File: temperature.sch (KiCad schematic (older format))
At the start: 20 parts, among them T1+1 TestPoint, T1-1 TestPoint, T2+1 TestPoint, T2-1 TestPoint, U4 ADS1118IDGS

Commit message: Debug routing
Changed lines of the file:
@@
 $Descr A4 11693 8268
 encoding utf-8
-Sheet 58 80
+Sheet 2 80
 Title "Acquisiton température"
 Date "2020-05-19"
@@
 AR Path="/5F466B56/5EB520F2" Ref="U34"  Part="1"
 AR Path="/5F466B61/5EB520F2" Ref="U35"  Part="1"
-F 0 "U35" H 7250 4400 50  0000 C CNN
+F 0 "U4" H 7250 4400 50  0000 C CNN
 F 1 "ADS1118IDGS" H 7250 4300 50  0000 C CNN
 F 2 "Package_SO:VSSOP-10_3x3mm_P0.5mm" H 6900 3750 50  0001 C CNN
@@
 AR Path="/5F466B56/5EC3D85A" Ref="C90"  Part="1"
 AR Path="/5F466B61/5EC3D85A" Ref="C97"  Part="1"
-F 0 "C97" H 5365 4896 50  0000 L CNN
+F 0 "C14" H 5365 4896 50  0000 L CNN
 F 1 "1uF" H 5365 4805 50  0000 L CNN
 F 2 "Capacitor_SMD:C_0402_1005Metric" H 5288 4700 50  0001 C CNN
@@
 AR Path="/5F466B56/5EC3D854" Ref="C88"  Part="1"
 AR Path="/5F466B61/5EC3D854" Ref="C95"  Part="1"
-F 0 "C95" H 5165 5346 50  0000 L CNN
+F 0 "C12" H 5165 5346 50  0000 L CNN
 F 1 "0.1uF" H 5165 5255 50  0000 L CNN
 F 2 "Capacitor_SMD:C_0402_1005Metric" H 5088 5150 50  0001 C CNN
@@
 AR Path="/5F466B56/5EC3D84E" Ref="C87"  Part="1"
 AR Path="/5F466B61/5EC3D84E" Ref="C94"  Part="1"
-F 0 "C94" H 4935 4354 50  0000 R CNN
+F 0 "C11" H 4935 4354 50  0000 R CNN
 F 1 "0.1uF" H 4935 4445 50  0000 R CNN
 F 2 "Capacitor_SMD:C_0402_1005Metric" H 5088 4250 50  0001 C CNN
@@
 AR Path="/5F466B56/5EC3D848" Ref="R116"  Part="1"
 AR Path="/5F466B61/5EC3D848" Ref="R124"  Part="1"
-F 0 "R124" V 4443 4650 50  0000 C CNN
+F 0 "R12" V 4443 4650 50  0000 C CNN
 F 1 "499" V 4534 4650 50  0000 C CNN
 F 2 "Resistor_SMD:R_0603_1608Metric" V 4580 4650 50  0001 C CNN
@@
 AR Path="/5F466B56/5EC3D842" Ref="R117"  Part="1"
 AR Path="/5F466B61/5EC3D842" Ref="R125"  Part="1"
-F 0 "R125" V 4443 5050 50  0000 C CNN
+F 0 "R13" V 4443 5050 50  0000 C CNN
 F 1 "499" V 4534 5050 50  0000 C CNN
 F 2 "Resistor_SMD:R_0603_1608Metric" V 4580 5050 50  0001 C CNN
@@
 AR Path="/5F466B56/5EC3D83C" Ref="R113"  Part="1"
 AR Path="/5F466B61/5EC3D83C" Ref="R121"  Part="1"
-F 0 "R121" H 4120 5346 50  0000 L CNN
+F 0 "R9" H 4120 5346 50  0000 L CNN
 F 1 "1M" H 4120 5255 50  0000 L CNN
 F 2 "Resistor_SMD:R_0805_2012Metric" V 3980 5300 50  0001 C CNN
@@
 AR Path="/5F466B56/5EC3D836" Ref="R112"  Part="1"
 AR Path="/5F466B61/5EC3D836" Ref="R120"  Part="1"
-F 0 "R120" H 4120 4446 50  0000 L CNN
+F 0 "R8" H 4120 4446 50  0000 L CNN
 F 1 "1M" H 4120 4355 50  0000 L CNN
 F 2 "Resistor_SMD:R_0805_2012Metric" V 3980 4400 50  0001 C CNN
@@
 AR Path="/5F466B56/5EBEC841" Ref="C91"  Part="1"
 AR Path="/5F466B61/5EBEC841" Ref="C98"  Part="1"
-F 0 "C98" H 6850 2950 50  0000 C CNN
+F 0 "C15" H 6850 2950 50  0000 C CNN
 F 1 "0.1uF" H 6850 3050 50  0000 C CNN
 F 2 "Capacitor_SMD:C_0402_1005Metric" H 6638 2850 50  0001 C CNN
@@
 AR Path="/5F466B56/5EC2636D" Ref="T2+7"  Part="1"
 AR Path="/5F466B61/5EC2636D" Ref="T2+8"  Part="1"
-F 0 "T2+8" H 4458 4368 50  0000 L CNN
+F 0 "T2+1" H 4458 4368 50  0000 L CNN
 F 1 "TestPoint" H 4458 4277 50  0000 L CNN
 F 2 "TestPoint:TestPoint_Pad_1.0x1.0mm" H 4600 4250 50  0001 C CNN
@@
 AR Path="/5F466B56/5EC467A6" Ref="T2-7"  Part="1"
 AR Path="/5F466B61/5EC467A6" Ref="T2-8"  Part="1"
-F 0 "T2-8" H 4050 5600 50  0000 L CNN
+F 0 "T2-1" H 4050 5600 50  0000 L CNN
 F 1 "TestPoint" H 4000 5500 50  0000 L CNN
 F 2 "TestPoint:TestPoint_Pad_1.0x1.0mm" H 4600 5450 50  0001 C CNN
@@
 AR Path="/5F466B56/5EC22011" Ref="T1-7"  Part="1"
 AR Path="/5F466B61/5EC22011" Ref="T1-8"  Part="1"
-F 0 "T1-8" H 4050 3500 50  0000 L CNN
+F 0 "T1-1" H 4050 3500 50  0000 L CNN
 F 1 "TestPoint" H 4000 3400 50  0000 L CNN
 F 2 "TestPoint:TestPoint_Pad_1.0x1.0mm" H 4600 3350 50  0001 C CNN
@@
 AR Path="/5F466B56/5EC1E92D" Ref="T1+7"  Part="1"
 AR Path="/5F466B61/5EC1E92D" Ref="T1+8"  Part="1"
-F 0 "T1+8" H 4458 2268 50  0000 L CNN
+F 0 "T1+1" H 4458 2268 50  0000 L CNN
 F 1 "TestPoint" H 4458 2177 50  0000 L CNN
 F 2 "TestPoint:TestPoint_Pad_1.0x1.0mm" H 4600 2150 50  0001 C CNN
@@
 AR Path="/5F466B56/5EC09C7B" Ref="R110"  Part="1"
 AR Path="/5F466B61/5EC09C7B" Ref="R118"  Part="1"
-F 0 "R118" H 4120 2346 50  0000 L CNN
+F 0 "R6" H 4120 2346 50  0000 L CNN
 F 1 "1M" H 4120 2255 50  0000 L CNN
 F 2 "Resistor_SMD:R_0805_2012Metric" V 3980 2300 50  0001 C CNN
@@
 AR Path="/5F466B56/5EC0F883" Ref="R111"  Part="1"
 AR Path="/5F466B61/5EC0F883" Ref="R119"  Part="1"
-F 0 "R119" H 4120 3246 50  0000 L CNN
+F 0 "R7" H 4120 3246 50  0000 L CNN
 F 1 "1M" H 4120 3155 50  0000 L CNN
 F 2 "Resistor_SMD:R_0805_2012Metric" V 3980 3200 50  0001 C CNN
@@
 AR Path="/5F466B56/5EC11D48" Ref="R115"  Part="1"
 AR Path="/5F466B61/5EC11D48" Ref="R123"  Part="1"
-F 0 "R123" V 4443 2950 50  0000 C CNN
+F 0 "R11" V 4443 2950 50  0000 C CNN
 F 1 "499" V 4534 2950 50  0000 C CNN
 F 2 "Resistor_SMD:R_0603_1608Metric" V 4580 2950 50  0001 C CNN
@@
 AR Path="/5F466B56/5EC12ACC" Ref="R114"  Part="1"
 AR Path="/5F466B61/5EC12ACC" Ref="R122"  Part="1"
-F 0 "R122" V 4443 2550 50  0000 C CNN
+F 0 "R10" V 4443 2550 50  0000 C CNN
 F 1 "499" V 4534 2550 50  0000 C CNN
 F 2 "Resistor_SMD:R_0603_1608Metric" V 4580 2550 50  0001 C CNN
@@
 AR Path="/5F466B56/5EC13396" Ref="C85"  Part="1"
 AR Path="/5F466B61/5EC13396" Ref="C92"  Part="1"
-F 0 "C92" H 4935 2254 50  0000 R CNN
+F 0 "C9" H 4935 2254 50  0000 R CNN
 F 1 "0.1uF" H 4935 2345 50  0000 R CNN
 F 2 "Capacitor_SMD:C_0402_1005Metric" H 5088 2150 50  0001 C CNN
@@
 AR Path="/5F466B56/5EC146F1" Ref="C86"  Part="1"
 AR Path="/5F466B61/5EC146F1" Ref="C93"  Part="1"
-F 0 "C93" H 5165 3246 50  0000 L CNN
+F 0 "C10" H 5165 3246 50  0000 L CNN
 F 1 "0.1uF" H 5165 3155 50  0000 L CNN
 F 2 "Capacitor_SMD:C_0402_1005Metric" H 5088 3050 50  0001 C CNN
@@
 AR Path="/5F466B56/5EC15202" Ref="C89"  Part="1"
 AR Path="/5F466B61/5EC15202" Ref="C96"  Part="1"
-F 0 "C96" H 5365 2796 50  0000 L CNN
+F 0 "C13" H 5365 2796 50  0000 L CNN
 F 1 "1uF" H 5365 2705 50  0000 L CNN
 F 2 "Capacitor_SMD:C_0402_1005Metric" H 5288 2600 50  0001 C CNN
@@
 AR Path="/5F466B56/618455B5" Ref="#PWR0188"  Part="1"
 AR Path="/5F466B61/618455B5" Ref="#PWR0196"  Part="1"
-F 0 "#PWR0196" H 6950 4200 50  0001 C CNN
+F 0 "#PWR028" H 6950 4200 50  0001 C CNN
 F 1 "GNDA" H 6955 4277 50  0000 C CNN
 F 2 "" H 6950 4450 50  0001 C CNN
@@
 AR Path="/5F466B56/61845768" Ref="#PWR0187"  Part="1"
 AR Path="/5F466B61/61845768" Ref="#PWR0195"  Part="1"
-F 0 "#PWR0195" H 6600 2900 50  0001 C CNN
+F 0 "#PWR027" H 6600 2900 50  0001 C CNN
 F 1 "GNDA" H 6605 2977 50  0000 C CNN
 F 2 "" H 6600 3150 50  0001 C CNN
@@
 AR Path="/5F466B56/61845B4A" Ref="#PWR0186"  Part="1"
 AR Path="/5F466B61/61845B4A" Ref="#PWR0194"  Part="1"
-F 0 "#PWR0194" H 5050 5200 50  0001 C CNN
+F 0 "#PWR026" H 5050 5200 50  0001 C CNN
 F 1 "GNDA" H 5055 5277 50  0000 C CNN
 F 2 "" H 5050 5450 50  0001 C CNN
@@
 AR Path="/5F466B56/61846A90" Ref="#PWR0182"  Part="1"
 AR Path="/5F466B61/61846A90" Ref="#PWR0190"  Part="1"
-F 0 "#PWR0190" H 4050 5200 50  0001 C CNN
+F 0 "#PWR022" H 4050 5200 50  0001 C CNN
 F 1 "GNDA" H 4055 5277 50  0000 C CNN
 F 2 "" H 4050 5450 50  0001 C CNN
@@
 AR Path="/5F466B56/61846F48" Ref="#PWR0184"  Part="1"
 AR Path="/5F466B61/61846F48" Ref="#PWR0192"  Part="1"
-F 0 "#PWR0192" H 5050 3100 50  0001 C CNN
+F 0 "#PWR024" H 5050 3100 50  0001 C CNN
 F 1 "GNDA" H 5055 3177 50  0000 C CNN
 F 2 "" H 5050 3350 50  0001 C CNN
@@
 AR Path="/5F466B56/618474E2" Ref="#PWR0181"  Part="1"
 AR Path="/5F466B61/618474E2" Ref="#PWR0189"  Part="1"
-F 0 "#PWR0189" H 4050 3100 50  0001 C CNN
+F 0 "#PWR021" H 4050 3100 50  0001 C CNN
 F 1 "GNDA" H 4055 3177 50  0000 C CNN
 F 2 "" H 4050 3350 50  0001 C CNN
@@
 AR Path="/5F466B56/6184779B" Ref="#PWR0185"  Part="1"
 AR Path="/5F466B61/6184779B" Ref="#PWR0193"  Part="1"
-F 0 "#PWR0193" H 5050 4000 50  0001 C CNN
+F 0 "#PWR025" H 5050 4000 50  0001 C CNN
 F 1 "GNDA" H 5055 4077 50  0000 C CNN
 F 2 "" H 5050 4250 50  0001 C CNN
@@
 AR Path="/5F466B56/6184B7DC" Ref="#PWR0183"  Part="1"
 AR Path="/5F466B61/6184B7DC" Ref="#PWR0191"  Part="1"
-F 0 "#PWR0191" H 5050 1900 50  0001 C CNN
+F 0 "#PWR023" H 5050 1900 50  0001 C CNN
 F 1 "GNDA" H 5055 1977 50  0000 C CNN
 F 2 "" H 5050 2150 50  0001 C CNN

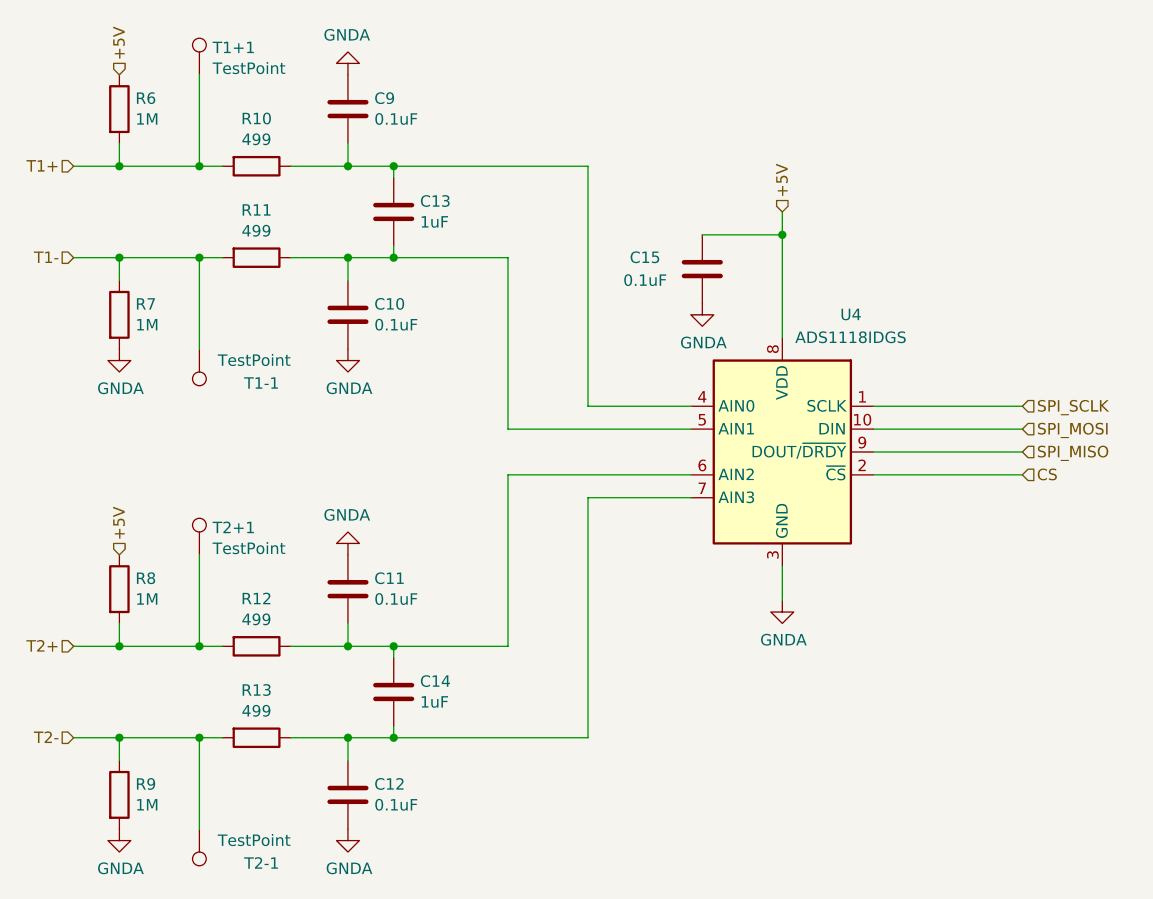
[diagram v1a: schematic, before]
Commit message: retrait des test points inutiles
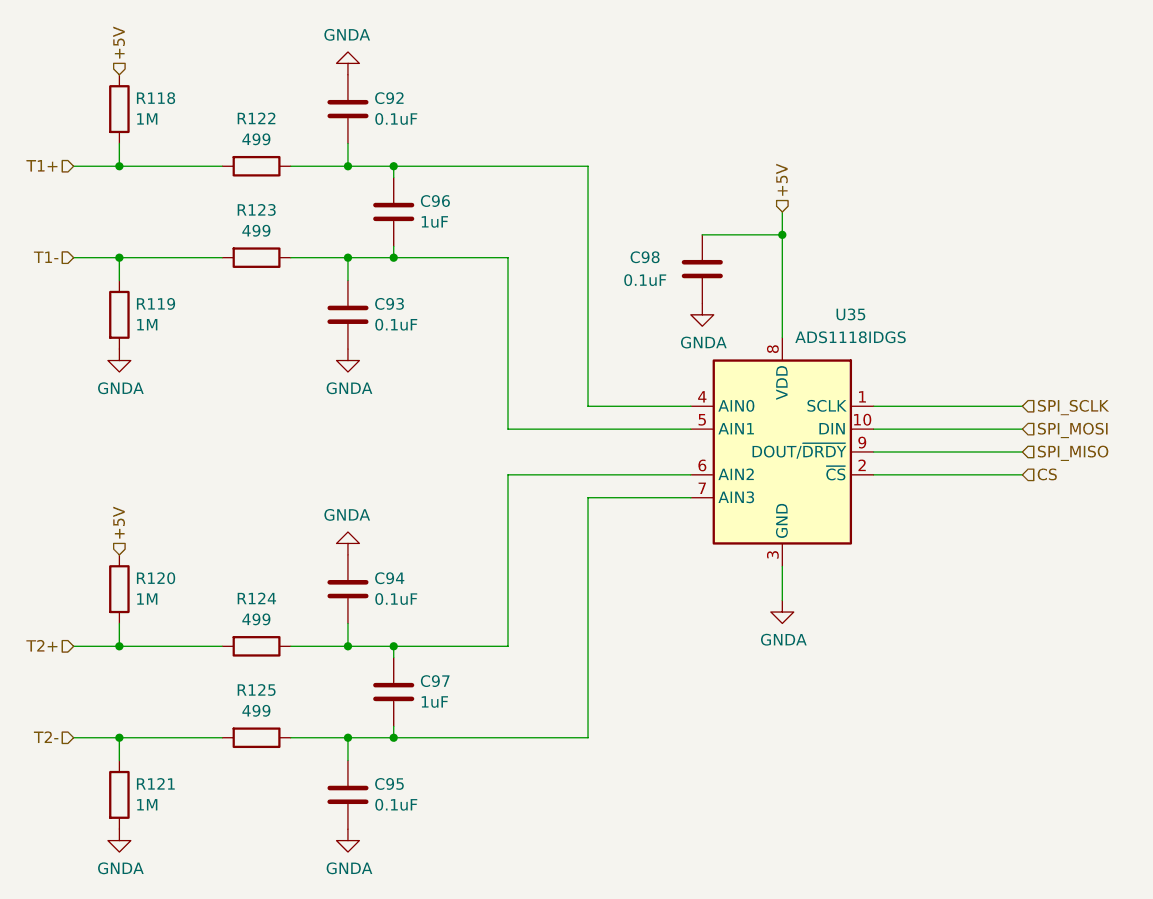
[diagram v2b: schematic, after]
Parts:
- removed T1+1, T1-1, T2+1, T2-1: TestPoint, TestPoint:TestPoint_Pad_1.0x1.0mm, symbol Connector:TestPoint

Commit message: Routed most of the power
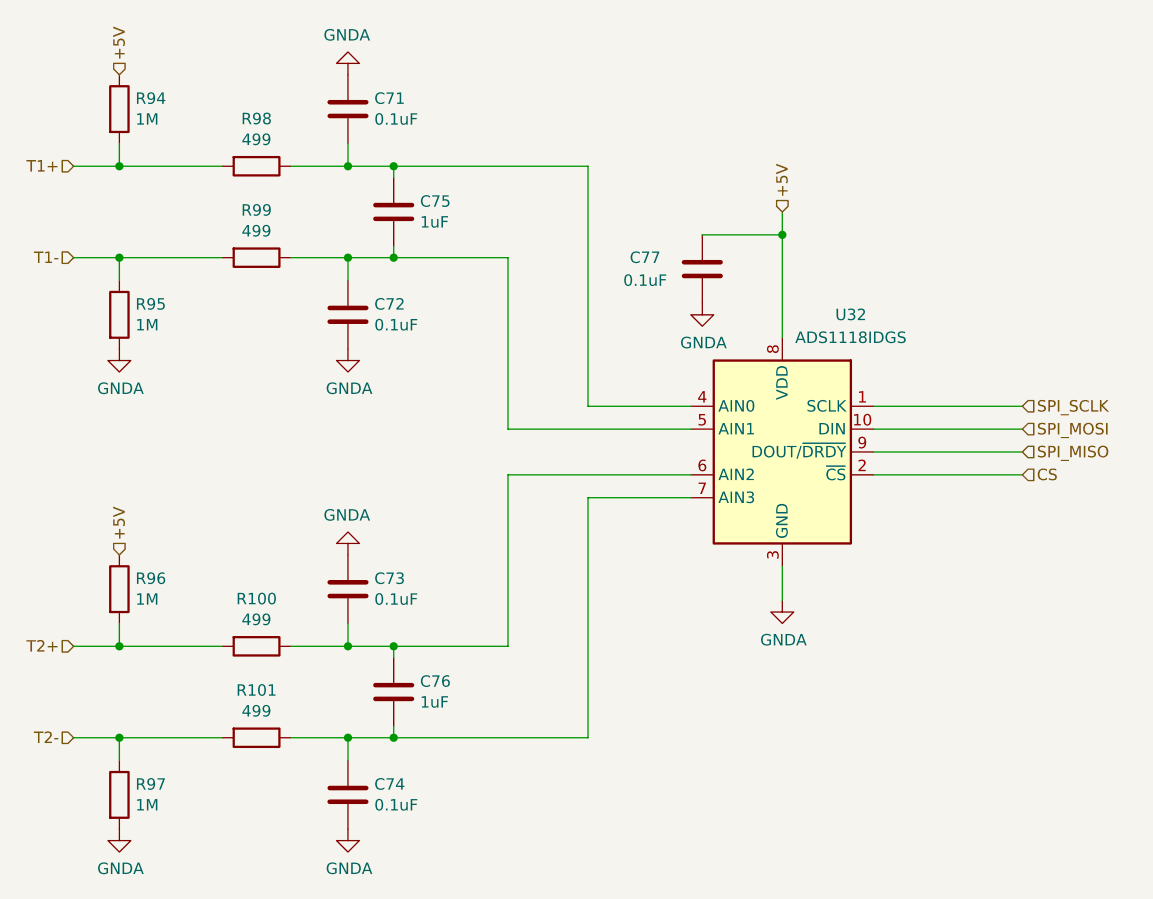
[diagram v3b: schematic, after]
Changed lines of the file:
@@
 $Descr A4 11693 8268
 encoding utf-8
-Sheet 2 80
+Sheet 55 80
 Title "Acquisiton température"
 Date "2020-05-19"
@@
 AR Path="/5F466B56/5EB520F2" Ref="U34"  Part="1"
 AR Path="/5F466B61/5EB520F2" Ref="U35"  Part="1"
-F 0 "U35" H 7250 4400 50  0000 C CNN
+F 0 "U32" H 7250 4400 50  0000 C CNN
 F 1 "ADS1118IDGS" H 7250 4300 50  0000 C CNN
 F 2 "Package_SO:VSSOP-10_3x3mm_P0.5mm" H 6900 3750 50  0001 C CNN
@@
 AR Path="/5F466B56/5EC3D85A" Ref="C90"  Part="1"
 AR Path="/5F466B61/5EC3D85A" Ref="C97"  Part="1"
-F 0 "C97" H 5365 4896 50  0000 L CNN
+F 0 "C76" H 5365 4896 50  0000 L CNN
 F 1 "1uF" H 5365 4805 50  0000 L CNN
 F 2 "Capacitor_SMD:C_0402_1005Metric" H 5288 4700 50  0001 C CNN
@@
 AR Path="/5F466B56/5EC3D854" Ref="C88"  Part="1"
 AR Path="/5F466B61/5EC3D854" Ref="C95"  Part="1"
-F 0 "C95" H 5165 5346 50  0000 L CNN
+F 0 "C74" H 5165 5346 50  0000 L CNN
 F 1 "0.1uF" H 5165 5255 50  0000 L CNN
 F 2 "Capacitor_SMD:C_0402_1005Metric" H 5088 5150 50  0001 C CNN
@@
 AR Path="/5F466B56/5EC3D84E" Ref="C87"  Part="1"
 AR Path="/5F466B61/5EC3D84E" Ref="C94"  Part="1"
-F 0 "C94" H 4935 4354 50  0000 R CNN
+F 0 "C73" H 4935 4354 50  0000 R CNN
 F 1 "0.1uF" H 4935 4445 50  0000 R CNN
 F 2 "Capacitor_SMD:C_0402_1005Metric" H 5088 4250 50  0001 C CNN
@@
 AR Path="/5F466B56/5EC3D848" Ref="R116"  Part="1"
 AR Path="/5F466B61/5EC3D848" Ref="R124"  Part="1"
-F 0 "R124" V 4443 4650 50  0000 C CNN
+F 0 "R100" V 4443 4650 50  0000 C CNN
 F 1 "499" V 4534 4650 50  0000 C CNN
 F 2 "Resistor_SMD:R_0603_1608Metric" V 4580 4650 50  0001 C CNN
@@
 AR Path="/5F466B56/5EC3D842" Ref="R117"  Part="1"
 AR Path="/5F466B61/5EC3D842" Ref="R125"  Part="1"
-F 0 "R125" V 4443 5050 50  0000 C CNN
+F 0 "R101" V 4443 5050 50  0000 C CNN
 F 1 "499" V 4534 5050 50  0000 C CNN
 F 2 "Resistor_SMD:R_0603_1608Metric" V 4580 5050 50  0001 C CNN
@@
 AR Path="/5F466B56/5EC3D83C" Ref="R113"  Part="1"
 AR Path="/5F466B61/5EC3D83C" Ref="R121"  Part="1"
-F 0 "R121" H 4120 5346 50  0000 L CNN
+F 0 "R97" H 4120 5346 50  0000 L CNN
 F 1 "1M" H 4120 5255 50  0000 L CNN
 F 2 "Resistor_SMD:R_0805_2012Metric" V 3980 5300 50  0001 C CNN
@@
 AR Path="/5F466B56/5EC3D836" Ref="R112"  Part="1"
 AR Path="/5F466B61/5EC3D836" Ref="R120"  Part="1"
-F 0 "R120" H 4120 4446 50  0000 L CNN
+F 0 "R96" H 4120 4446 50  0000 L CNN
 F 1 "1M" H 4120 4355 50  0000 L CNN
 F 2 "Resistor_SMD:R_0805_2012Metric" V 3980 4400 50  0001 C CNN
@@
 AR Path="/5F466B56/5EBEC841" Ref="C91"  Part="1"
 AR Path="/5F466B61/5EBEC841" Ref="C98"  Part="1"
-F 0 "C98" H 6850 2950 50  0000 C CNN
+F 0 "C77" H 6850 2950 50  0000 C CNN
 F 1 "0.1uF" H 6850 3050 50  0000 C CNN
 F 2 "Capacitor_SMD:C_0402_1005Metric" H 6638 2850 50  0001 C CNN
@@
 AR Path="/5F466B56/5EC09C7B" Ref="R110"  Part="1"
 AR Path="/5F466B61/5EC09C7B" Ref="R118"  Part="1"
-F 0 "R118" H 4120 2346 50  0000 L CNN
+F 0 "R94" H 4120 2346 50  0000 L CNN
 F 1 "1M" H 4120 2255 50  0000 L CNN
 F 2 "Resistor_SMD:R_0805_2012Metric" V 3980 2300 50  0001 C CNN
@@
 AR Path="/5F466B56/5EC0F883" Ref="R111"  Part="1"
 AR Path="/5F466B61/5EC0F883" Ref="R119"  Part="1"
-F 0 "R119" H 4120 3246 50  0000 L CNN
+F 0 "R95" H 4120 3246 50  0000 L CNN
 F 1 "1M" H 4120 3155 50  0000 L CNN
 F 2 "Resistor_SMD:R_0805_2012Metric" V 3980 3200 50  0001 C CNN
@@
 AR Path="/5F466B56/5EC11D48" Ref="R115"  Part="1"
 AR Path="/5F466B61/5EC11D48" Ref="R123"  Part="1"
-F 0 "R123" V 4443 2950 50  0000 C CNN
+F 0 "R99" V 4443 2950 50  0000 C CNN
 F 1 "499" V 4534 2950 50  0000 C CNN
 F 2 "Resistor_SMD:R_0603_1608Metric" V 4580 2950 50  0001 C CNN
@@
 AR Path="/5F466B56/5EC12ACC" Ref="R114"  Part="1"
 AR Path="/5F466B61/5EC12ACC" Ref="R122"  Part="1"
-F 0 "R122" V 4443 2550 50  0000 C CNN
+F 0 "R98" V 4443 2550 50  0000 C CNN
 F 1 "499" V 4534 2550 50  0000 C CNN
 F 2 "Resistor_SMD:R_0603_1608Metric" V 4580 2550 50  0001 C CNN
@@
 AR Path="/5F466B56/5EC13396" Ref="C85"  Part="1"
 AR Path="/5F466B61/5EC13396" Ref="C92"  Part="1"
-F 0 "C92" H 4935 2254 50  0000 R CNN
+F 0 "C71" H 4935 2254 50  0000 R CNN
 F 1 "0.1uF" H 4935 2345 50  0000 R CNN
 F 2 "Capacitor_SMD:C_0402_1005Metric" H 5088 2150 50  0001 C CNN
@@
 AR Path="/5F466B56/5EC146F1" Ref="C86"  Part="1"
 AR Path="/5F466B61/5EC146F1" Ref="C93"  Part="1"
-F 0 "C93" H 5165 3246 50  0000 L CNN
+F 0 "C72" H 5165 3246 50  0000 L CNN
 F 1 "0.1uF" H 5165 3155 50  0000 L CNN
 F 2 "Capacitor_SMD:C_0402_1005Metric" H 5088 3050 50  0001 C CNN
@@
 AR Path="/5F466B56/5EC15202" Ref="C89"  Part="1"
 AR Path="/5F466B61/5EC15202" Ref="C96"  Part="1"
-F 0 "C96" H 5365 2796 50  0000 L CNN
+F 0 "C75" H 5365 2796 50  0000 L CNN
 F 1 "1uF" H 5365 2705 50  0000 L CNN
 F 2 "Capacitor_SMD:C_0402_1005Metric" H 5288 2600 50  0001 C CNN
@@
 AR Path="/5F466B56/618455B5" Ref="#PWR0188"  Part="1"
 AR Path="/5F466B61/618455B5" Ref="#PWR0196"  Part="1"
-F 0 "#PWR0196" H 6950 4200 50  0001 C CNN
+F 0 "#PWR0172" H 6950 4200 50  0001 C CNN
 F 1 "GNDA" H 6955 4277 50  0000 C CNN
 F 2 "" H 6950 4450 50  0001 C CNN
@@
 AR Path="/5F466B56/61845768" Ref="#PWR0187"  Part="1"
 AR Path="/5F466B61/61845768" Ref="#PWR0195"  Part="1"
-F 0 "#PWR0195" H 6600 2900 50  0001 C CNN
+F 0 "#PWR0171" H 6600 2900 50  0001 C CNN
 F 1 "GNDA" H 6605 2977 50  0000 C CNN
 F 2 "" H 6600 3150 50  0001 C CNN
@@
 AR Path="/5F466B56/61845B4A" Ref="#PWR0186"  Part="1"
 AR Path="/5F466B61/61845B4A" Ref="#PWR0194"  Part="1"
-F 0 "#PWR0194" H 5050 5200 50  0001 C CNN
+F 0 "#PWR0170" H 5050 5200 50  0001 C CNN
 F 1 "GNDA" H 5055 5277 50  0000 C CNN
 F 2 "" H 5050 5450 50  0001 C CNN
@@
 AR Path="/5F466B56/61846A90" Ref="#PWR0182"  Part="1"
 AR Path="/5F466B61/61846A90" Ref="#PWR0190"  Part="1"
-F 0 "#PWR0190" H 4050 5200 50  0001 C CNN
+F 0 "#PWR0166" H 4050 5200 50  0001 C CNN
 F 1 "GNDA" H 4055 5277 50  0000 C CNN
 F 2 "" H 4050 5450 50  0001 C CNN
@@
 AR Path="/5F466B56/61846F48" Ref="#PWR0184"  Part="1"
 AR Path="/5F466B61/61846F48" Ref="#PWR0192"  Part="1"
-F 0 "#PWR0192" H 5050 3100 50  0001 C CNN
+F 0 "#PWR0168" H 5050 3100 50  0001 C CNN
 F 1 "GNDA" H 5055 3177 50  0000 C CNN
 F 2 "" H 5050 3350 50  0001 C CNN
@@
 AR Path="/5F466B56/618474E2" Ref="#PWR0181"  Part="1"
 AR Path="/5F466B61/618474E2" Ref="#PWR0189"  Part="1"
-F 0 "#PWR0189" H 4050 3100 50  0001 C CNN
+F 0 "#PWR0165" H 4050 3100 50  0001 C CNN
 F 1 "GNDA" H 4055 3177 50  0000 C CNN
 F 2 "" H 4050 3350 50  0001 C CNN
@@
 AR Path="/5F466B56/6184779B" Ref="#PWR0185"  Part="1"
 AR Path="/5F466B61/6184779B" Ref="#PWR0193"  Part="1"
-F 0 "#PWR0193" H 5050 4000 50  0001 C CNN
+F 0 "#PWR0169" H 5050 4000 50  0001 C CNN
 F 1 "GNDA" H 5055 4077 50  0000 C CNN
 F 2 "" H 5050 4250 50  0001 C CNN
@@
 AR Path="/5F466B56/6184B7DC" Ref="#PWR0183"  Part="1"
 AR Path="/5F466B61/6184B7DC" Ref="#PWR0191"  Part="1"
-F 0 "#PWR0191" H 5050 1900 50  0001 C CNN
+F 0 "#PWR0167" H 5050 1900 50  0001 C CNN
 F 1 "GNDA" H 5055 1977 50  0000 C CNN
 F 2 "" H 5050 2150 50  0001 C CNN
